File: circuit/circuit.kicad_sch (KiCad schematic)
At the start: 33 parts, among them J1 USB_A, J2 Conn_02x03_Counter_Clockwise, U1 RP2040, U2 AMS1117-3.3, U3 W25Q32JVSS, U4 W25Q32JVSS, Y1 12MHz

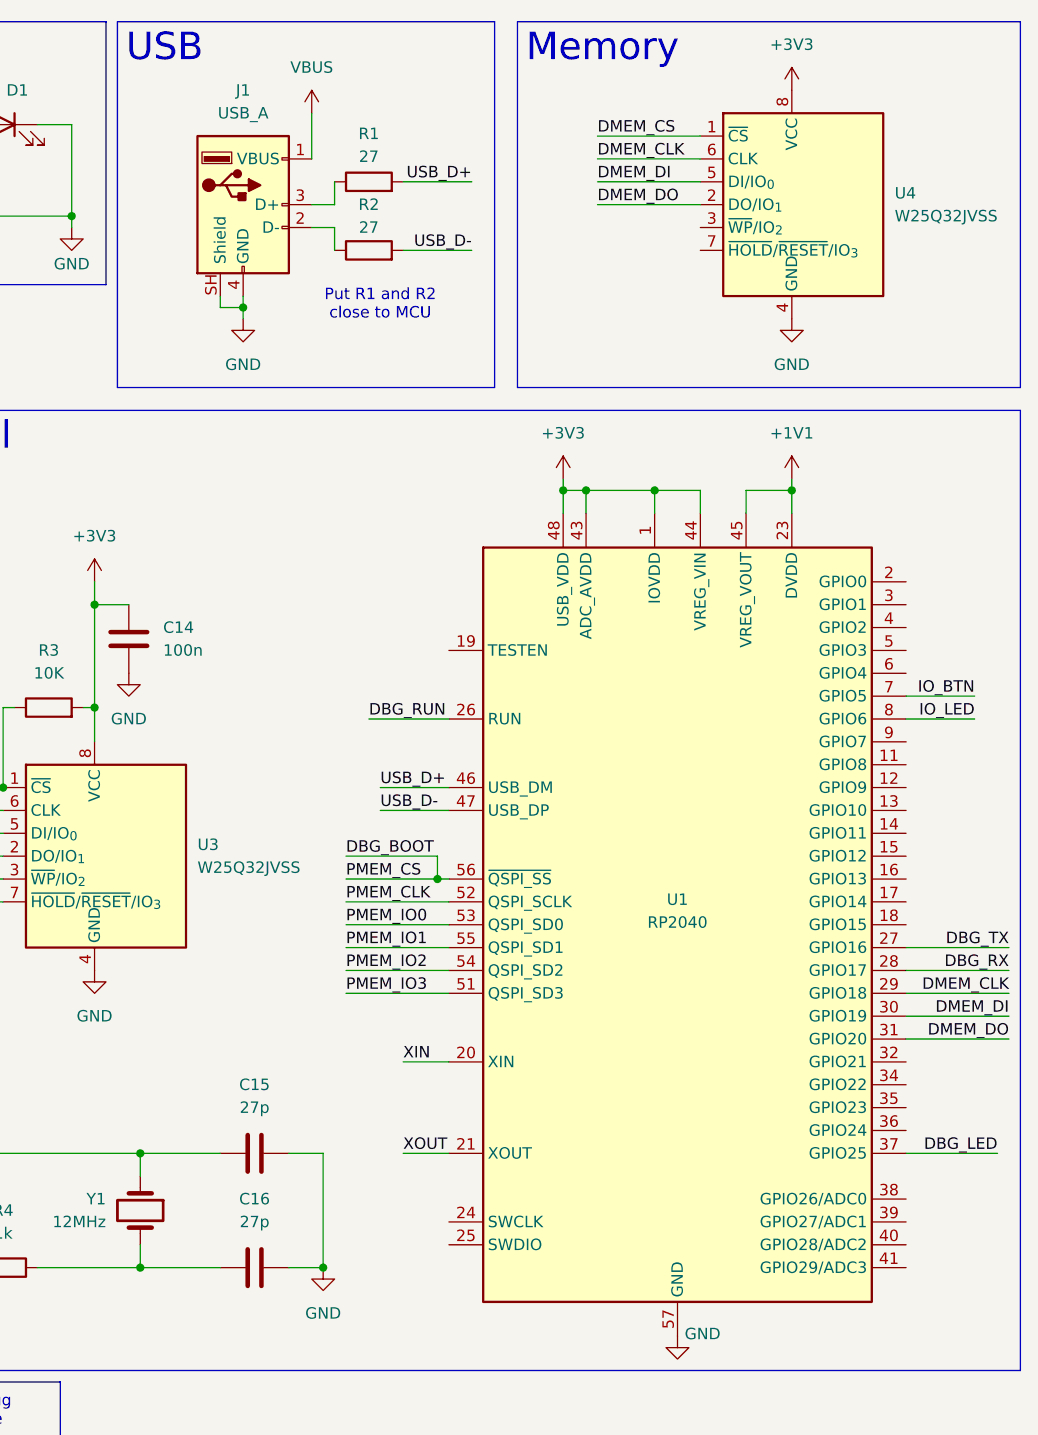
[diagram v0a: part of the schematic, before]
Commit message: Fix ERC errors
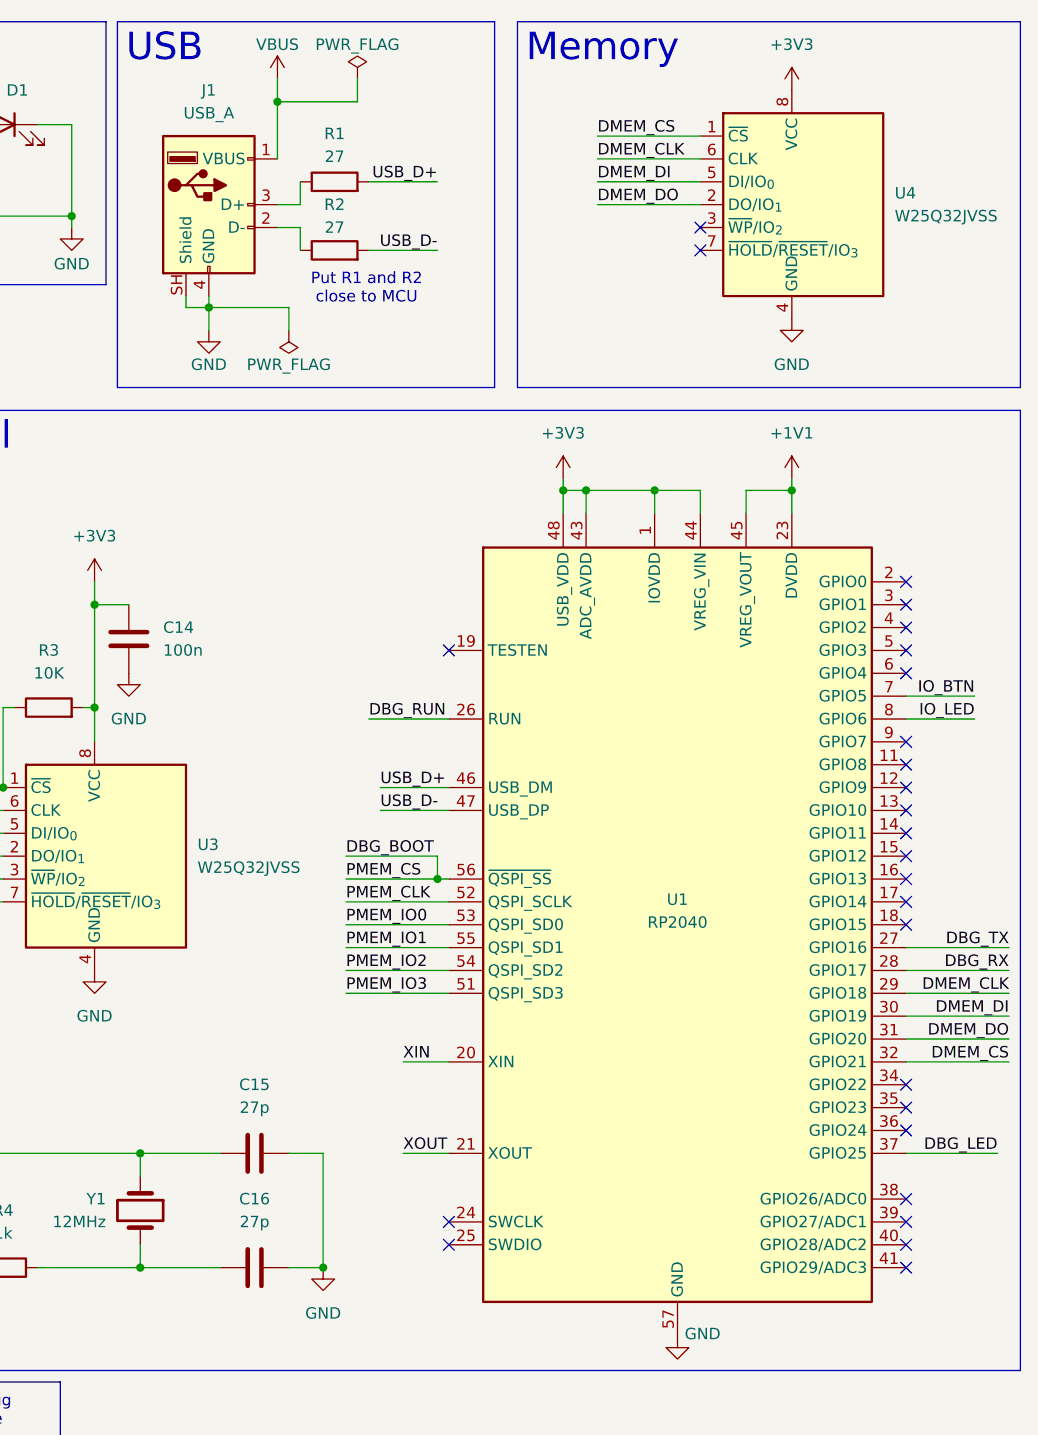
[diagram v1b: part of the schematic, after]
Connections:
- net DMEM_CS: now also U1.32 (GPIO21)
- no-connect marks 0 -> 26
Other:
- moved on the sheet: J1, R1, R2

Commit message: specify components
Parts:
- C1, C10, C11, C12, C13, C14, C15, C16, C2, C3, C4, C5, C6, C7, C8, C9: footprint (none) -> Capacitor_SMD:C_0805_2012Metric
- D1: footprint (none) -> LED_THT:LED_D5.0mm
- J1: footprint (none) -> Connector_USB:USB_A_CNCTech_1001-011-01101_Horizontal
- J2: value Conn_02x03_Counter_Clockwise -> (none); footprint (none) -> Connector_PinSocket_2.54mm:PinSocket_2x03_P2.54mm_Horizontal
- R1, R2, R3, R4, R5, R6, R7, R8: footprint (none) -> Resistor_SMD:R_0805_2012Metric
- SW1: footprint (none) -> Button_Switch_THT:SW_PUSH_6mm_H5mm
- Y1: footprint (none) -> Crystal:Crystal_SMD_SeikoEpson_FA238-4Pin_3.2x2.5mm
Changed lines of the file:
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@@
 			)
 		)
-		(property "Footprint" ""
+		(property "Footprint" "LED_THT:LED_D5.0mm"
 			(at 170.18 25.4 0)
 			(hide yes)
@@
 			)
 		)
-		(property "Footprint" ""
+		(property "Footprint" "Resistor_SMD:R_0805_2012Metric"
 			(at 138.43 193.548 90)
 			(hide yes)
@@
 			)
 		)
-		(property "Footprint" ""
+		(property "Footprint" "Crystal:Crystal_SMD_SeikoEpson_FA238-4Pin_3.2x2.5mm"
 			(at 185.42 146.05 0)
 			(hide yes)
@@
 			)
 		)
-		(property "Footprint" ""
+		(property "Footprint" "Capacitor_SMD:C_0805_2012Metric"
 			(at 78.4352 158.75 0)
 			(hide yes)
@@
 			)
 		)
-		(property "Footprint" ""
+		(property "Footprint" "Capacitor_SMD:C_0805_2012Metric"
 			(at 30.1752 158.75 0)
 			(hide yes)
@@
 			)
 		)
-		(property "Footprint" ""
+		(property "Footprint" "Capacitor_SMD:C_0805_2012Metric"
 			(at 83.5152 184.15 0)
 			(hide yes)
@@
 			)
 		)
-		(property "Footprint" ""
+		(property "Footprint" "Resistor_SMD:R_0805_2012Metric"
 			(at 160.02 179.832 90)
 			(hide yes)
@@
 			)
 		)
-		(property "Footprint" ""
+		(property "Footprint" "Capacitor_SMD:C_0805_2012Metric"
 			(at 105.1052 184.15 0)
 			(hide yes)
@@
 			)
 		)
-		(property "Footprint" ""
+		(property "Footprint" "Capacitor_SMD:C_0805_2012Metric"
 			(at 194.31 138.7348 0)
 			(hide yes)
@@
 			)
 		)
-		(property "Footprint" ""
+		(property "Footprint" "Capacitor_SMD:C_0805_2012Metric"
 			(at 185.1152 86.36 0)
 			(hide yes)
@@
 			)
 		)
-		(property "Footprint" ""
+		(property "Footprint" "Capacitor_SMD:C_0805_2012Metric"
 			(at 18.7452 158.75 0)
 			(hide yes)
@@
 			)
 		)
-		(property "Footprint" ""
+		(property "Footprint" "Connector_USB:USB_A_CNCTech_1001-011-01101_Horizontal"
 			(at 196.85 35.56 0)
 			(hide yes)
@@
 			)
 		)
-		(property "Footprint" ""
+		(property "Footprint" "Capacitor_SMD:C_0805_2012Metric"
 			(at 103.8352 158.75 0)
 			(hide yes)
@@
 			)
 		)
-		(property "Footprint" ""
+		(property "Footprint" "Resistor_SMD:R_0805_2012Metric"
 			(at 170.18 154.178 90)
 			(hide yes)
@@
 			)
 		)
-		(property "Footprint" ""
+		(property "Footprint" "Capacitor_SMD:C_0805_2012Metric"
 			(at 41.6052 158.75 0)
 			(hide yes)
@@
 			)
 		)
-		(property "Footprint" ""
+		(property "Footprint" "Resistor_SMD:R_0805_2012Metric"
 			(at 207.01 33.528 90)
 			(hide yes)
@@
 			)
 		)
-		(property "Footprint" ""
+		(property "Footprint" "Button_Switch_THT:SW_PUSH_6mm_H5mm"
 			(at 163.83 30.48 0)
 			(hide yes)
@@
 			)
 		)
-		(property "Value" "Conn_02x03_Counter_Clockwise"
+		(property "Value" ""
 			(at 149.86 177.8 0)
 			(hide yes)
@@
 			)
 		)
-		(property "Footprint" ""
+		(property "Footprint" "Connector_PinSocket_2.54mm:PinSocket_2x03_P2.54mm_Horizontal"
 			(at 148.59 184.15 0)
 			(hide yes)
@@
 			)
 		)
-		(property "Footprint" ""
+		(property "Footprint" "Capacitor_SMD:C_0805_2012Metric"
 			(at 89.8652 158.75 0)
 			(hide yes)
@@
 			)
 		)
-		(property "Footprint" ""
+		(property "Footprint" "Resistor_SMD:R_0805_2012Metric"
 			(at 162.56 27.178 90)
 			(hide yes)
@@
 			)
 		)
-		(property "Footprint" ""
+		(property "Footprint" "Capacitor_SMD:C_0805_2012Metric"
 			(at 93.6752 184.15 0)
 			(hide yes)
@@
 			)
 		)
-		(property "Footprint" ""
+		(property "Footprint" "Capacitor_SMD:C_0805_2012Metric"
 			(at 27.6352 184.15 0)
 			(hide yes)
@@
 			)
 		)
-		(property "Footprint" ""
+		(property "Footprint" "Capacitor_SMD:C_0805_2012Metric"
 			(at 67.0052 158.75 0)
 			(hide yes)
@@
 			)
 		)
-		(property "Footprint" ""
+		(property "Footprint" "Resistor_SMD:R_0805_2012Metric"
 			(at 207.01 41.148 90)
 			(hide yes)
@@
 			)
 		)
-		(property "Footprint" ""
+		(property "Footprint" "Capacitor_SMD:C_0805_2012Metric"
 			(at 56.8452 184.15 0)
 			(hide yes)
@@
 			)
 		)
-		(property "Footprint" ""
+		(property "Footprint" "Capacitor_SMD:C_0805_2012Metric"
 			(at 54.3052 158.75 0)
 			(hide yes)
@@
 			)
 		)
-		(property "Footprint" ""
+		(property "Footprint" "Resistor_SMD:R_0805_2012Metric"
 			(at 139.7 185.928 90)
 			(hide yes)
@@
 			)
 		)
-		(property "Footprint" ""
+		(property "Footprint" "Capacitor_SMD:C_0805_2012Metric"
 			(at 194.31 151.4348 0)
 			(hide yes)
@@
 			)
 		)
-		(property "Footprint" ""
+		(property "Footprint" "Resistor_SMD:R_0805_2012Metric"
 			(at 175.26 91.948 90)
 			(hide yes)
